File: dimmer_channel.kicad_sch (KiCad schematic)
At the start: 16 parts

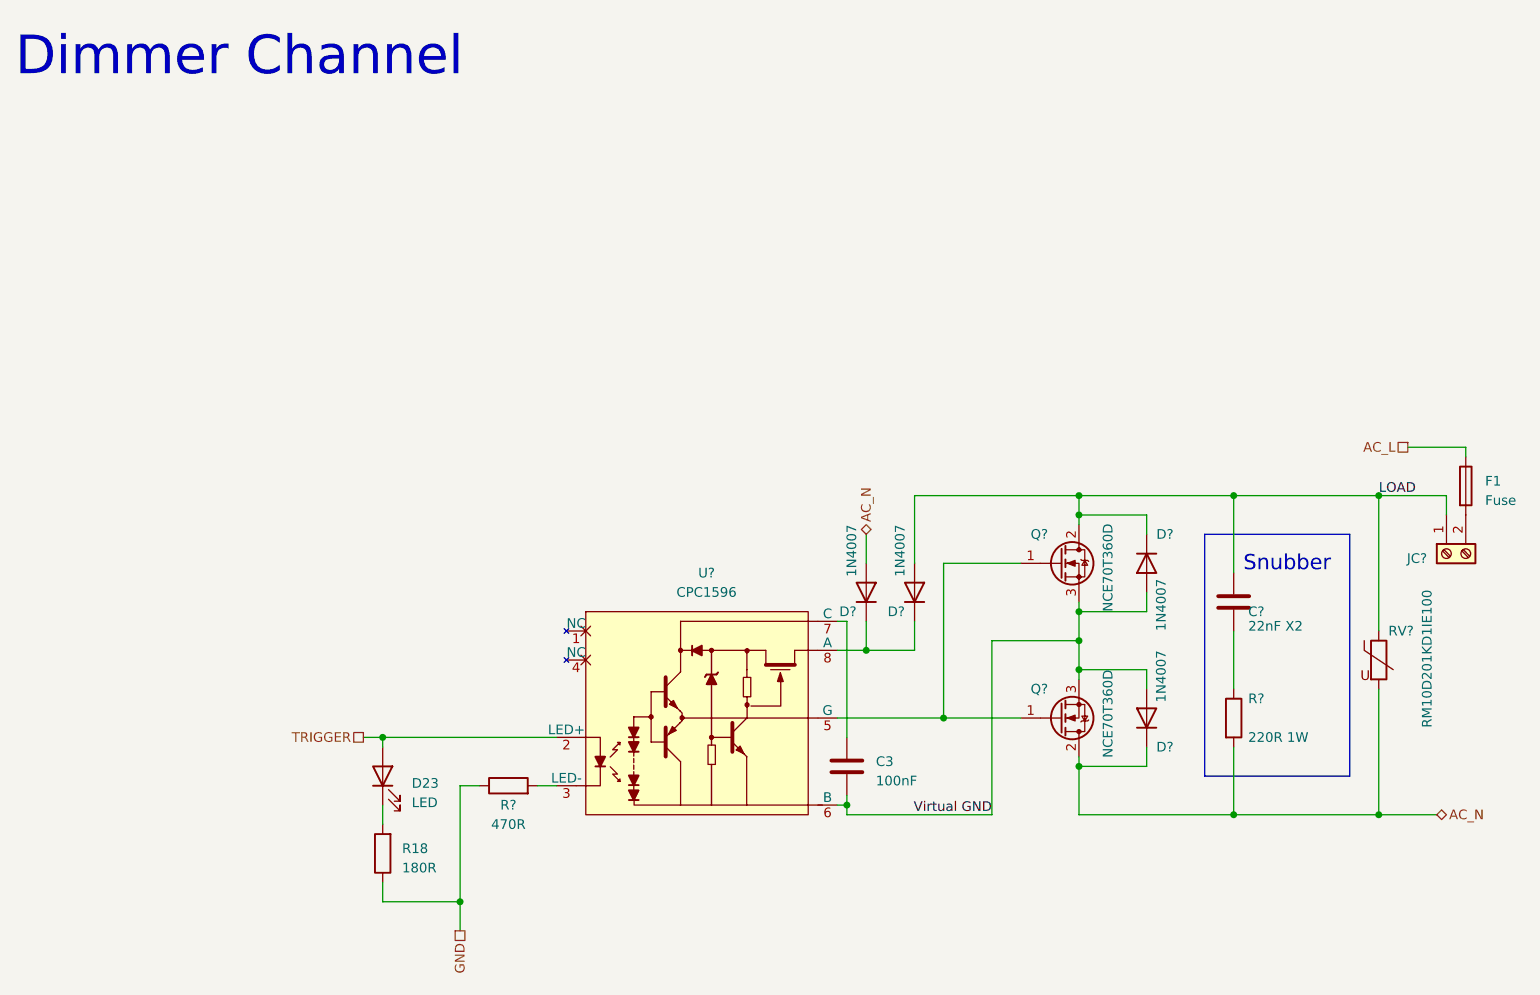
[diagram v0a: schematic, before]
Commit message: Added changes based on Tim Williams feedback on StackExchange.
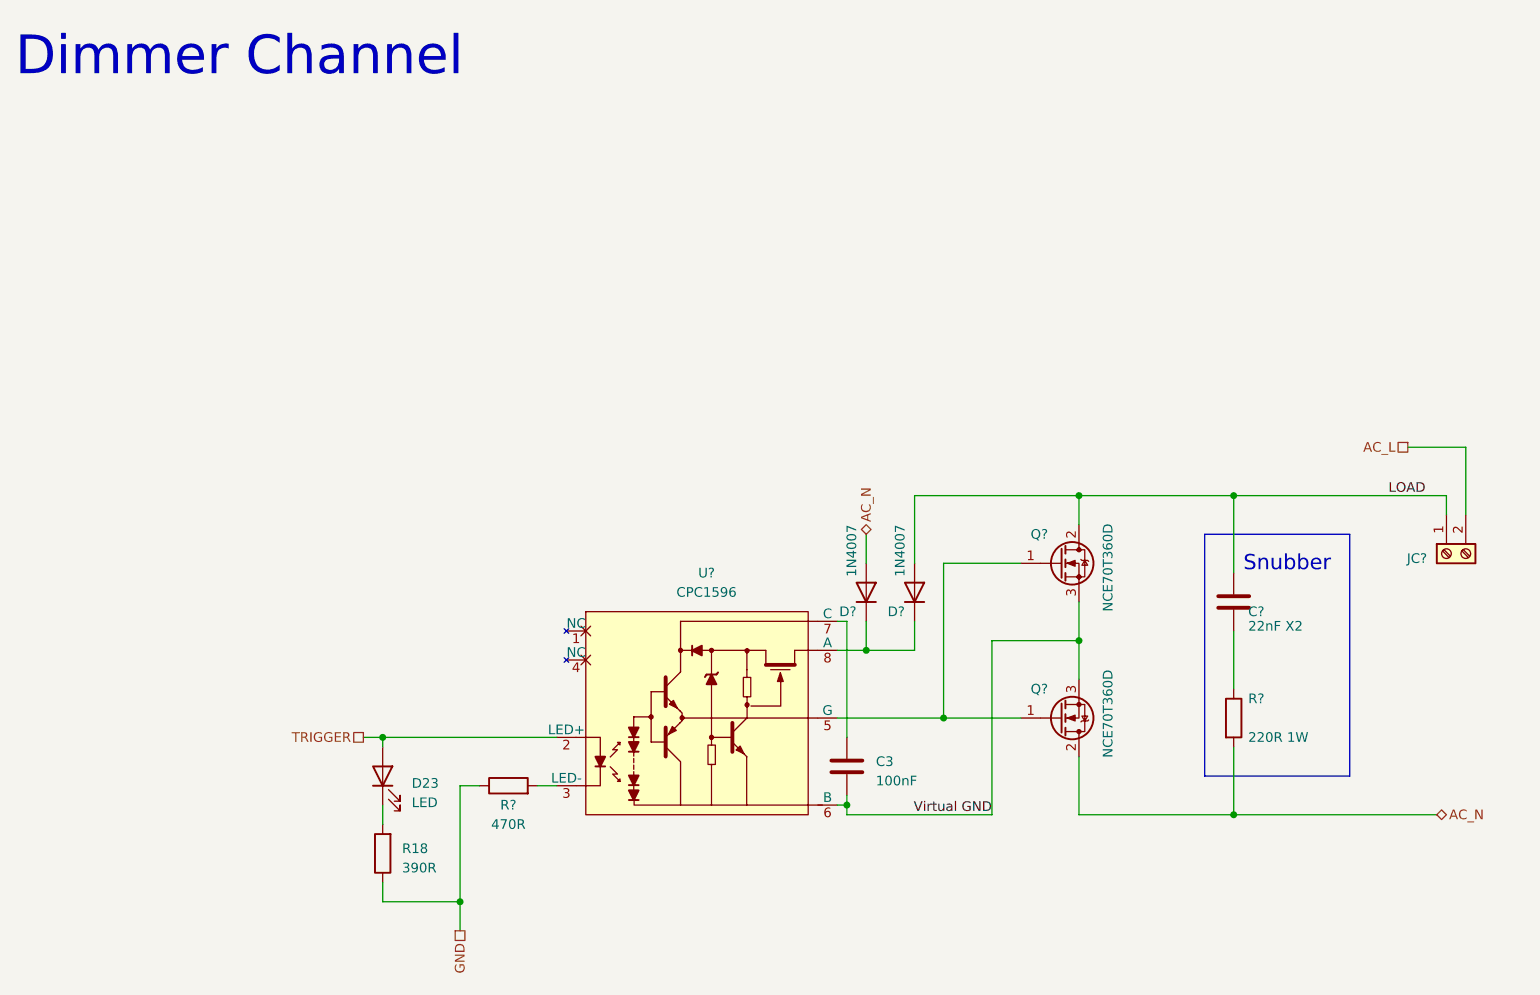
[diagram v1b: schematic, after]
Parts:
- removed D? (x2): 1N4007, Diode_SMD:D_SMA, symbol Diode:1N4007
- removed F1: Fuse, Fuse:Fuseholder_Cylinder-5x20mm_Schurter_0031_8201_Horizontal_Open, symbol Device:Fuse
- removed RV?: RM10D201KD1IE100, Varistor:RV_Disc_D12mm_W3.9mm_P7.5mm, symbol Device:Varistor
- R18: value 180R -> 390R; LCSC C137585 -> C17655
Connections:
- net AC_L: now also JC?.2 (Pin_2)

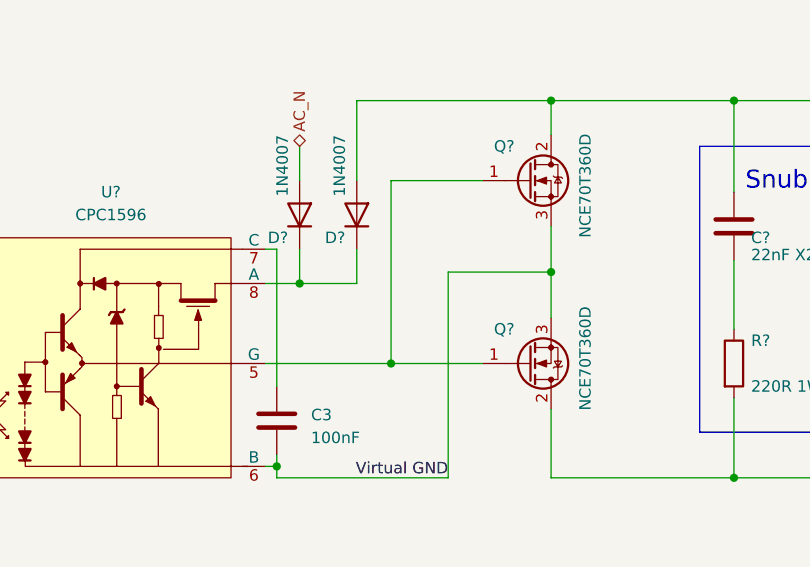
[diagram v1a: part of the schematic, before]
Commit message: Added some test points. Added RS-485 Module. Updated PBC.
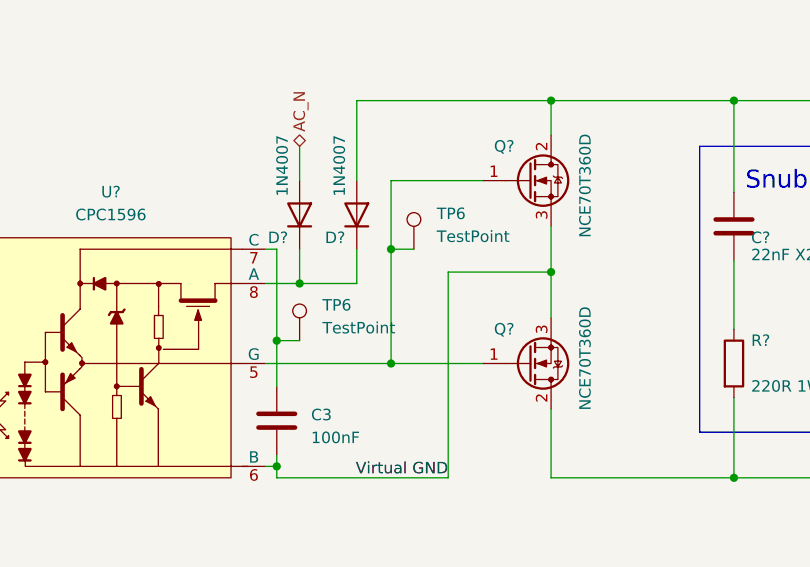
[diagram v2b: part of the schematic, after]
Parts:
- added TP6 (x2): TestPoint, TestPoint:TestPoint_THTPad_D2.0mm_Drill1.0mm, symbol Connector:TestPoint
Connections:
- net at Q?.1 (G), Q?.1 (G), U?.5 (G): now also TP6.1
- net at C3.1, U?.7 (C): now also TP6.1
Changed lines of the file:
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@@
   (junction (at 180.34 124.46) (diameter 0) (color 0 0 0 0)
   )
+  (junction (at 142.24 99.06) (diameter 0) (color 0 0 0 0)
+  )
   (junction (at 129.54 123.19) (diameter 0) (color 0 0 0 0)
   )
@@
   (junction (at 68.58 114.3) (diameter 0) (color 0 0 0 0)
   )
+  (junction (at 129.54 109.22) (diameter 0) (color 0 0 0 0)
+  )
   (junction (at 160.02 82.55) (diameter 0) (color 0 0 0 0)
   )
@@
     (stroke (width 0) (type default))
   )
+  (wire (pts (xy 142.24 99.06) (xy 142.24 111.76))
+    (stroke (width 0) (type default))
+  )
   (wire (pts (xy 88.9 120.65) (xy 91.44 120.65))
     (stroke (width 0) (type default))
@@
     (stroke (width 0) (type default))
   )
+  (wire (pts (xy 129.54 109.22) (xy 132.08 109.22))
+    (stroke (width 0) (type default))
+  )
   (wire (pts (xy 180.34 82.55) (xy 208.28 82.55))
     (stroke (width 0) (type default))
@@
     (stroke (width 0) (type default))
   )
+  (wire (pts (xy 142.24 99.06) (xy 144.78 99.06))
+    (stroke (width 0) (type default))
+  )
   (wire (pts (xy 129.54 124.46) (xy 129.54 123.19))
     (stroke (width 0) (type default))
@@
     (stroke (width 0) (type default))
   )
+  (wire (pts (xy 129.54 109.22) (xy 129.54 114.3))
+    (stroke (width 0) (type default))
+  )
   (polyline (pts (xy 176.53 87.63) (xy 176.53 119.38))
     (stroke (width 0) (type default))
@@
     (stroke (width 0) (type default))
   )
-  (wire (pts (xy 142.24 91.44) (xy 142.24 111.76))
+  (wire (pts (xy 142.24 91.44) (xy 142.24 99.06))
     (stroke (width 0) (type default))
   )
@@
     (stroke (width 0) (type default))
   )
-  (wire (pts (xy 129.54 99.06) (xy 129.54 114.3))
+  (wire (pts (xy 129.54 99.06) (xy 129.54 109.22))
     (stroke (width 0) (type default))
   )
@@
         (path "/71908919-2b0a-47a6-84be-12fefaa6e518/98a309c1-fab9-489e-9fd7-11d34f76e4b1"
           (reference "R20") (unit 1)
+        )
+      )
+    )
+  )
+  (symbol (lib_id "Connector:TestPoint") (at 144.78 99.06 0) (unit 1)
+    (in_bom yes) (on_board yes) (dnp no) (fields_autoplaced)
+    (property "Reference" "TP6" (at 147.32 95.123 0)
+      (effects (font (size 1.27 1.27)) (justify left))
+    )
+    (property "Value" "TestPoint" (at 147.32 97.663 0)
+      (effects (font (size 1.27 1.27)) (justify left))
+    )
+    (property "Footprint" "TestPoint:TestPoint_THTPad_D2.0mm_Drill1.0mm" (at 149.86 99.06 0)
+      (effects (font (size 1.27 1.27)) hide)
+    )
+    (property "Datasheet" "~" (at 149.86 99.06 0)
+      (effects (font (size 1.27 1.27)) hide)
+    )
+    (pin "1")
+    (instances
+      (project "Rev1"
+        (path "/71908919-2b0a-47a6-84be-12fefaa6e518"
+          (reference "TP6") (unit 1)
+        )
+        (path "/71908919-2b0a-47a6-84be-12fefaa6e518/5081f111-7078-43b0-82cf-1fe66b064440"
+          (reference "TP7") (unit 1)
+        )
+        (path "/71908919-2b0a-47a6-84be-12fefaa6e518/f3321929-b732-4933-8aa2-aecb179f7b16"
+          (reference "TP13") (unit 1)
+        )
+        (path "/71908919-2b0a-47a6-84be-12fefaa6e518/63a7502f-87e1-4005-93d7-2007d3c6eab7"
+          (reference "TP14") (unit 1)
+        )
+        (path "/71908919-2b0a-47a6-84be-12fefaa6e518/45cb508d-a23b-4fc4-bc4b-418ece1135aa"
+          (reference "TP15") (unit 1)
+        )
+        (path "/71908919-2b0a-47a6-84be-12fefaa6e518/df7cf28b-cf21-48af-84fb-010c4b52f77a"
+          (reference "TP16") (unit 1)
+        )
+        (path "/71908919-2b0a-47a6-84be-12fefaa6e518/98a309c1-fab9-489e-9fd7-11d34f76e4b1"
+          (reference "TP17") (unit 1)
         )
       )
@@
         )
       )
+    )
+  )
+  (symbol (lib_id "Connector:TestPoint") (at 132.08 109.22 0) (unit 1)
+    (in_bom yes) (on_board yes) (dnp no) (fields_autoplaced)
+    (property "Reference" "TP6" (at 134.62 105.283 0)
+      (effects (font (size 1.27 1.27)) (justify left))
+    )
+    (property "Value" "TestPoint" (at 134.62 107.823 0)
+      (effects (font (size 1.27 1.27)) (justify left))
+    )
+    (property "Footprint" "TestPoint:TestPoint_THTPad_D2.0mm_Drill1.0mm" (at 137.16 109.22 0)
+      (effects (font (size 1.27 1.27)) hide)
+    )
+    (property "Datasheet" "~" (at 137.16 109.22 0)
+      (effects (font (size 1.27 1.27)) hide)
+    )
+    (pin "1")
+    (instances
+      (project "Rev1"
+        (path "/71908919-2b0a-47a6-84be-12fefaa6e518"
+          (reference "TP6") (unit 1)
+        )
+        (path "/71908919-2b0a-47a6-84be-12fefaa6e518/5081f111-7078-43b0-82cf-1fe66b064440"
+          (reference "TP7") (unit 1)
+        )
+        (path "/71908919-2b0a-47a6-84be-12fefaa6e518/f3321929-b732-4933-8aa2-aecb179f7b16"
+          (reference "TP8") (unit 1)
+        )
+        (path "/71908919-2b0a-47a6-84be-12fefaa6e518/63a7502f-87e1-4005-93d7-2007d3c6eab7"
+          (reference "TP9") (unit 1)
+        )
+        (path "/71908919-2b0a-47a6-84be-12fefaa6e518/45cb508d-a23b-4fc4-bc4b-418ece1135aa"
+          (reference "TP10") (unit 1)
+        )
+        (path "/71908919-2b0a-47a6-84be-12fefaa6e518/df7cf28b-cf21-48af-84fb-010c4b52f77a"
+          (reference "TP11") (unit 1)
+        )
+        (path "/71908919-2b0a-47a6-84be-12fefaa6e518/98a309c1-fab9-489e-9fd7-11d34f76e4b1"
+          (reference "TP12") (unit 1)
+        )
+      )
